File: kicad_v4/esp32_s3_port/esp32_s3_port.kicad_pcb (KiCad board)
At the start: 2 copper layers, 144.8 x 108.6 mm, 48 parts, among them J1 AudioJack4, J2 AudioJack4, SW1 KS33_SW_HS, SW10 KS33_SW_HS, SW11 KS33_SW_HS, SW12 KS33_SW_HS, SW13 KS33_SW_HS, SW14 KS33_SW_HS, SW15 KS33_SW_HS, SW16 KS33_SW_HS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

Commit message: ssd 1306
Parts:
- added Brd1: SSD1306, SSD1306:128x64OLED, F.Cu at (154.1, 80.5)
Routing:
- net VCC: track 0.00 -> 38.9 mm
- net SDA: track 0.00 -> 21.1 mm, vias 0 -> 1
- net SCL: track 0.00 -> 20.6 mm, vias 0 -> 1

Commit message: battery switch
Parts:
- added SW22: Slide_Switch_SPDT_P3mm_10x5x10mm, PCM_SL_Devices:Slide_Switch_SPDT_P3mm_10x5x10mm, F.Cu at (159.5, 110.0)
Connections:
- U1 pad 3: Net-(BT1-+) -> Net-(U1-BAT)
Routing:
- net Net-(U1-BAT): track 0.00 -> 17.0 mm
- net Net-(BT1-+): track 4.47 -> 16.3 mm

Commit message: updates
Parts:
- removed J2: AudioJack4, PJ-320A_Library:PJ-320A
- removed JP1: JUP_P5.08mm, PCM_SL_Jumpers:JUP_P5.08mm
- added J3: misc Pogo pin connector, Connector_PinHeader_2.54mm:PinHeader_1x04_P2.54mm_Vertical, F.Cu at (163.8, 84.5)
- J1: value AudioJack4 -> Battery; footprint PJ-320A_Library:PJ-320A -> Connector_PinHeader_2.54mm:PinHeader_1x02_P2.54mm_Vertical; moved to F.Cu
- moved J1 26.2 mm to (154.3, 109.8), turned to 0 degrees
- moved Brd1 20.4 mm to (156.7, 100.8), turned to 0 degrees
- moved R2 12.8 mm to (146.7, 109.9)
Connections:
- A1 pad 1: TX -> unconnected-(A1-D1/TX-Pad1)
- A1 pad 2: RX -> unconnected-(A1-D0/RX-Pad2)
- A1 pad 27: VBUS -> unconnected-(A1-VUSB/5V-Pad27)
- J1 pad 1: GND -> Net-(J1-Pad1)
- J1 pad 2: VBUS -> GND
- SW22 pad 2: Net-(BT1-+) -> Net-(J1-Pad1)
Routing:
- net SDA: track 21.1 -> 53.2 mm, vias 1 -> 2
- net VBUS: track 31.5 -> 0.00 mm, vias 1 -> 0
- net SCL: track 20.6 -> 51.1 mm, vias 1 -> 2
- net VCC: track 38.9 -> 65.8 mm, vias 0 -> 1
- net RX: track 23.4 -> 0.00 mm
- net TX: track 23.3 -> 0.00 mm
- net Net-(BT1-+): track 16.3 -> 0.00 mm
- net Net-(J1-Pad1): track 0.00 -> 6.50 mm
- net Net-(U1-PROG): track 8.67 -> 14.3 mm
- net /finished: track 49.2 -> 51.0 mm
- net /charging: track 61.7 -> 62.8 mm
- net GND: vias 16 -> 19

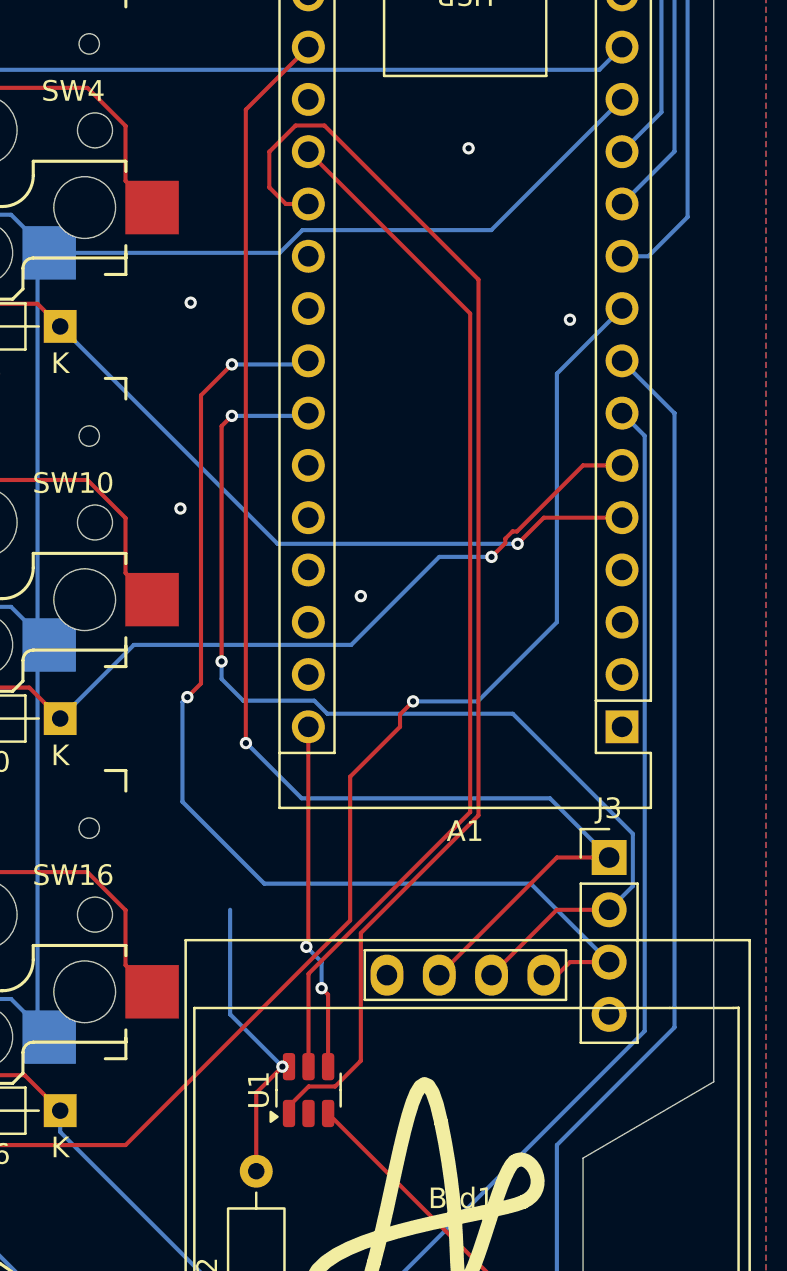
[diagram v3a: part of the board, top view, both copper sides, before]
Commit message: hardware update
lots of items were switced with the equivalent headers
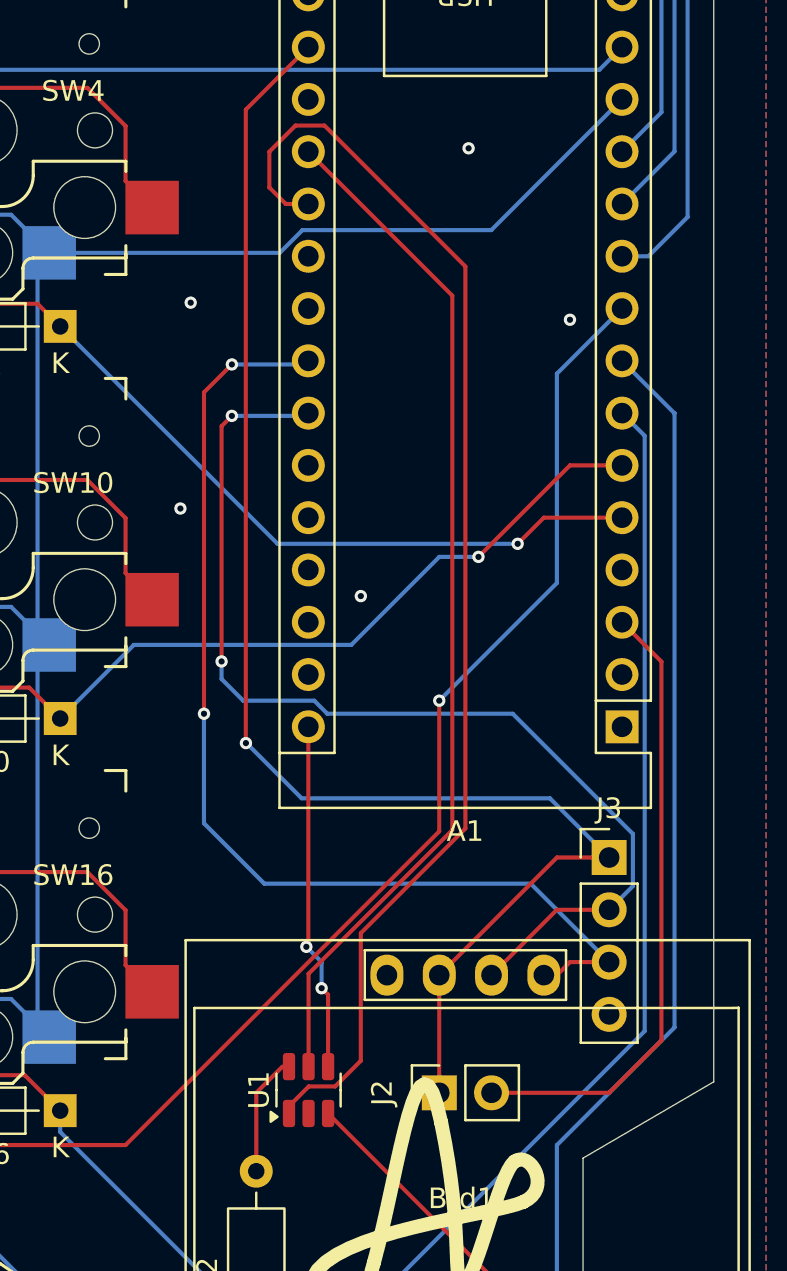
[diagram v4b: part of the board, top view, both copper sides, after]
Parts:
- added J2: PINHD_1x2_Female, Connector_PinSocket_2.54mm:PinSocket_1x02_P2.54mm_Vertical, F.Cu at (155.6, 95.9)
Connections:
- A1 pad 3: unconnected-(A1-~{RESET}-Pad3) -> Net-(A1-~{RESET})
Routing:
- net Net-(A1-~{RESET}): track 0.00 -> 30.4 mm
- net Net-(U1-PROG): track 14.3 -> 5.61 mm, vias 1 -> 0
- net VCC: track 65.8 -> 71.6 mm
- net /Col1: track 226.1 -> 224.3 mm
- net /finished: track 51.0 -> 50.2 mm
- net SDA: track 53.2 -> 52.6 mm
- net /charging: track 62.8 -> 62.3 mm

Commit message: surface mount version
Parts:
- added Main-mirrored1: Arduino_Nano_ESP32, Module:Arduino_Nano, B.Cu at (149.2, 78.1)
- moved Main1 3.17 mm to (161.3, 78.1)
- renumbered A1 to Main1
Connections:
- net Net-(A1-~{RESET}) renamed /Rst
- Main1 pad 27: unconnected-(A1-VUSB/5V-Pad27) -> +5V
- Main1 pad 30: +5V -> unconnected-(Main1-VIN-Pad30)
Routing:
- net +5V: track 17.0 -> 50.9 mm
- net /finished: track 50.2 -> 66.8 mm, vias 0 -> 2
- net /Row4: track 125.7 -> 141.2 mm
- net /charging: track 62.3 -> 72.9 mm, vias 0 -> 2
- net /Row3: track 175.4 -> 166.9 mm, vias 1 -> 2
- net /Rst: track 30.4 -> 38.3 mm
- net VCC: track 71.6 -> 78.2 mm, vias 1 -> 0
- net /Col1: track 224.3 -> 230.3 mm, vias 4 -> 3
- net /Col3: track 226.4 -> 221.3 mm
- net /Row1: track 142.9 -> 138.7 mm, vias 1 -> 0
- net /Col6: track 89.0 -> 85.9 mm
- net /Col5: track 170.5 -> 167.3 mm
- net /Col2: track 203.8 -> 200.8 mm
- net /Row2: track 140.4 -> 143.1 mm, vias 1 -> 2
- net SDA: track 52.6 -> 54.5 mm, vias 2 -> 0
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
